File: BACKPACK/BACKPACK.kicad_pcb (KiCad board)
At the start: 4 copper layers, 70.8 x 45 mm, 30 parts, among them J1 Conn_01x03_Pin, J2 Conn_01x03_Pin, J3 Conn_01x03_Pin, J4 Conn_Coaxial, J5 Conn_02x08_Odd_Even, J6 Conn_02x08_Odd_Even, J7 Conn_01x03_Pin, SW1 BOOTSEL, SW2 RESET, U10 RAK3172, U9 TESEO-LIV4F

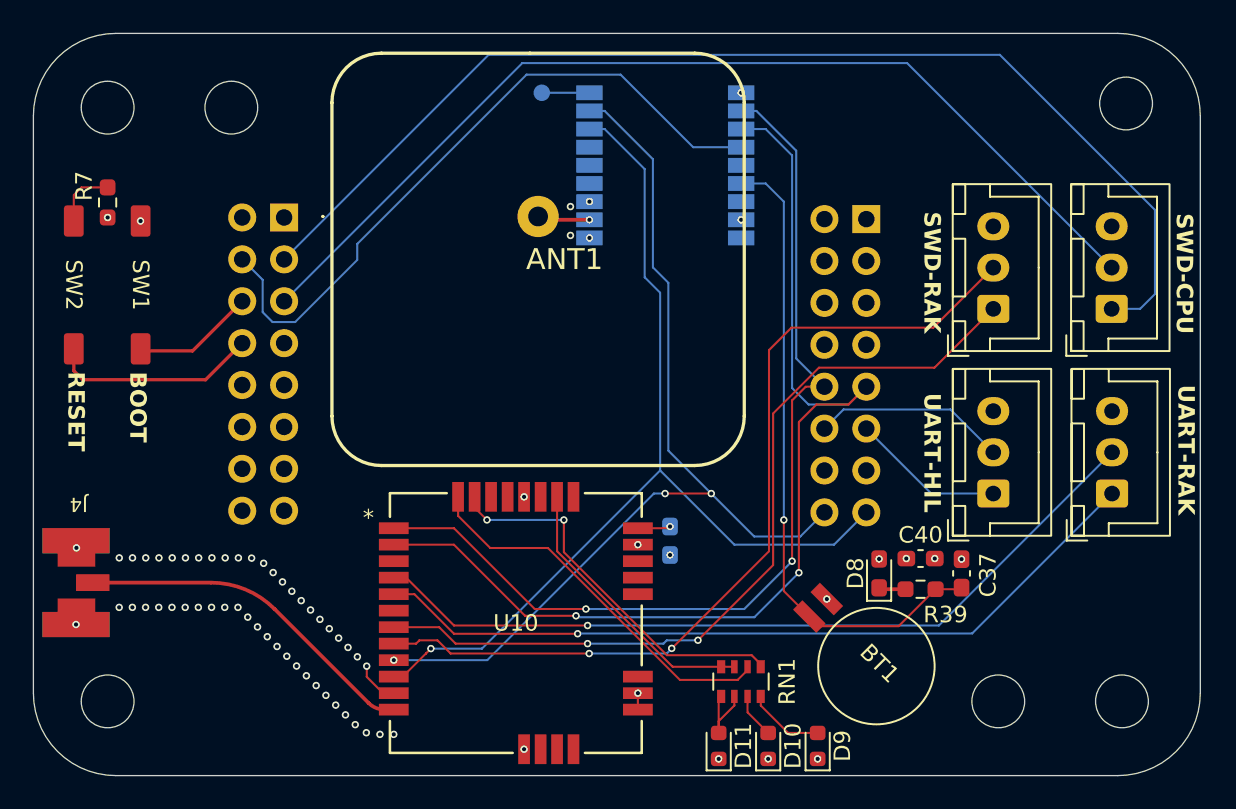
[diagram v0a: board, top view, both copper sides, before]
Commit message: constrains fix
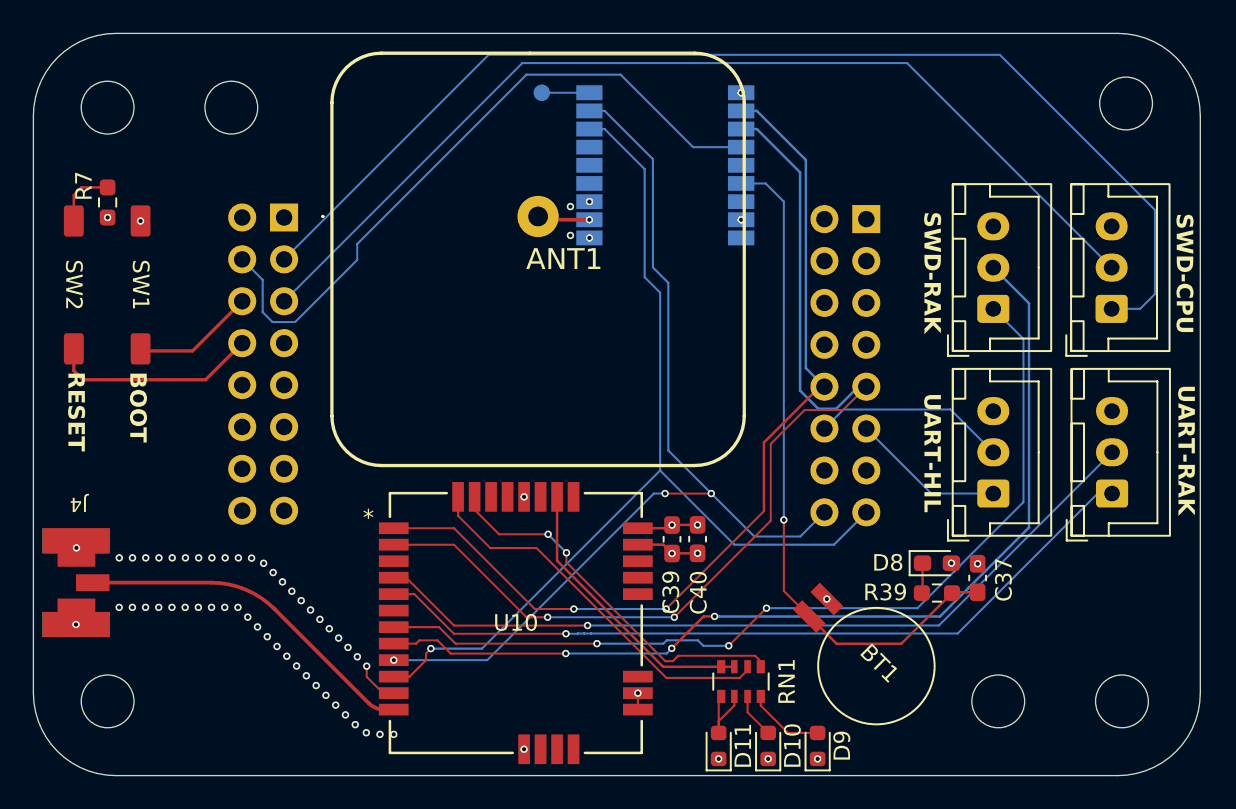
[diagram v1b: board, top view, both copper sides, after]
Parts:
- added G***: LOGO, LOGO, B.Cu at (158.1, 88.8)
- added G***: LOGO, LOGO, B.Cu at (180.2, 70.3)
- C39: moved to F.Cu
- moved C40 13.6 mm to (166.8, 96.2), turned to -90 degrees
- moved D8 3.56 mm to (181.3, 97.6), turned to 0 degrees
- moved R39 1.02 mm to (181.3, 99.4)
- moved C37 1.01 mm to (183.8, 98.5)
- moved C39 0.15 mm to (165.2, 96.2)
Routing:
- net /SWCLK: track 53.6 -> 58.7 mm, vias 2 -> 3
- net /SWDIO: track 50.6 -> 54.9 mm, vias 2 -> 3
- net GND: track 3.70 -> 7.54 mm, vias 67 -> 66
- net /TX_GPS: track 58.8 -> 55.5 mm
- net /RX_GPS: track 64.8 -> 61.9 mm
- net Net-(BT1-+): track 39.3 -> 41.0 mm
- net +3V3: track 2.15 -> 3.70 mm

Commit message: fine rev 2.2
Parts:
- H1, H2, H3, H4, H5, H6: moved to B.Cu
- J5, J6: moved to F.Cu
- moved H4 61.5 mm to (131.0, 106.0), turned to 180 degrees
- moved H3 61.0 mm to (192.0, 106.0), turned to 180 degrees
- moved H5 47.0 mm to (138.0, 106.0), turned to 180 degrees
- moved H6 46.5 mm to (185.0, 70.0), turned to 180 degrees
- moved J6 22.7 mm to (141.7, 99.3)
- moved J5 22.7 mm to (177.0, 99.4)
- moved BT1 5.88 mm to (179.5, 102.6)
- moved SW2 4.25 mm to (133.2, 80.8)
- moved SW1 3.90 mm to (129.1, 80.8)
- moved H2 0.79 mm to (192.0, 70.0), turned to 180 degrees
- turned H1 to 180 degrees
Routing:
- net /CPU_SWDIO: track 61.3 -> 80.1 mm, vias 0 -> 1
- net /CPU_SWDCLK: track 69.9 -> 87.6 mm, vias 0 -> 1
- net PPS: track 41.6 -> 54.4 mm, vias 0 -> 1
- net GND: track 7.54 -> 18.3 mm, vias 66 -> 64
- net /BOOTSEL: track 7.89 -> 15.6 mm
- net /TX_GPS: track 55.5 -> 62.6 mm
- net Net-(BT1-+): track 41.0 -> 47.8 mm
- net /RX_GPS: track 61.9 -> 59.2 mm
- net HIL_RX: track 11.8 -> 13.6 mm, vias 0 -> 1
- net /RESET: track 12.7 -> 11.2 mm
- net /SDA_RADIO: track 59.8 -> 58.5 mm, vias 1 -> 2
- net HIL_TX: track 9.33 -> 10.5 mm, vias 0 -> 1
- net ANT: track 21.1 -> 20.5 mm
- net +3V3: vias 4 -> 5

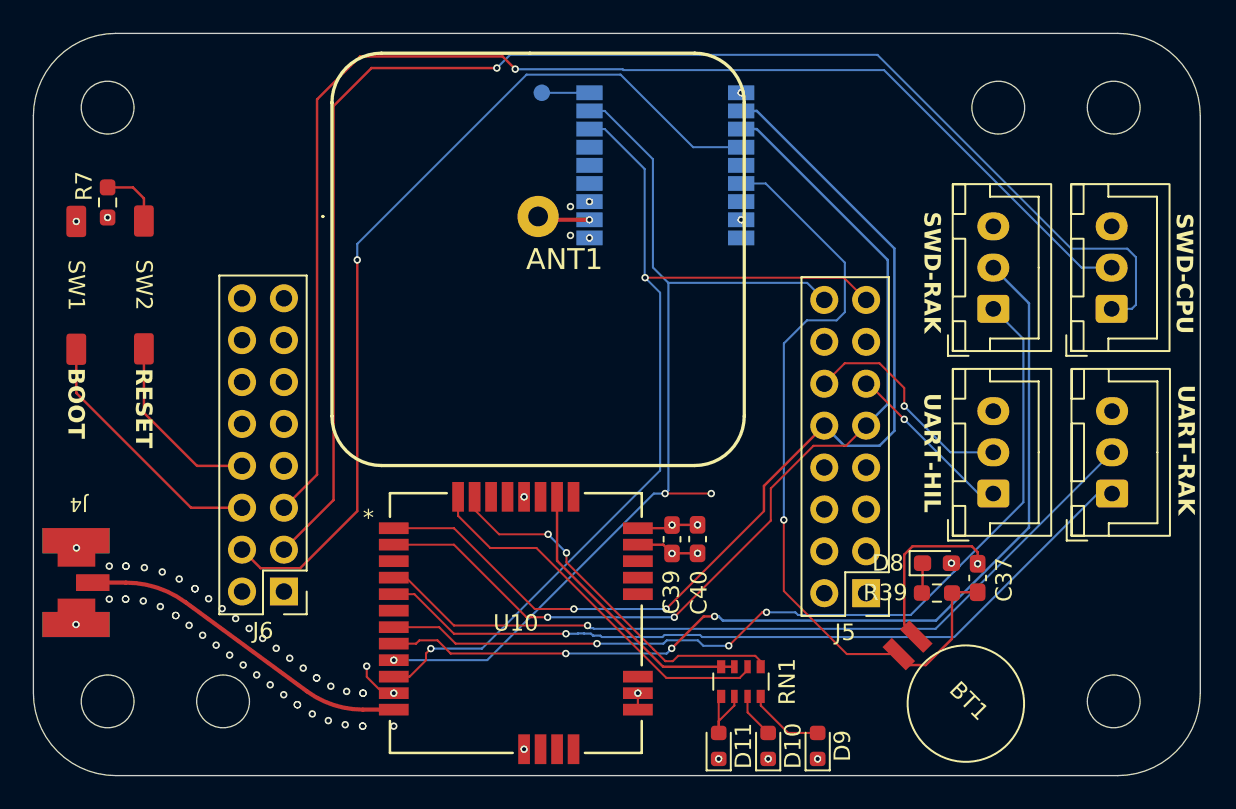
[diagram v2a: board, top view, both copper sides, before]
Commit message: Aggiunta GNDPlane
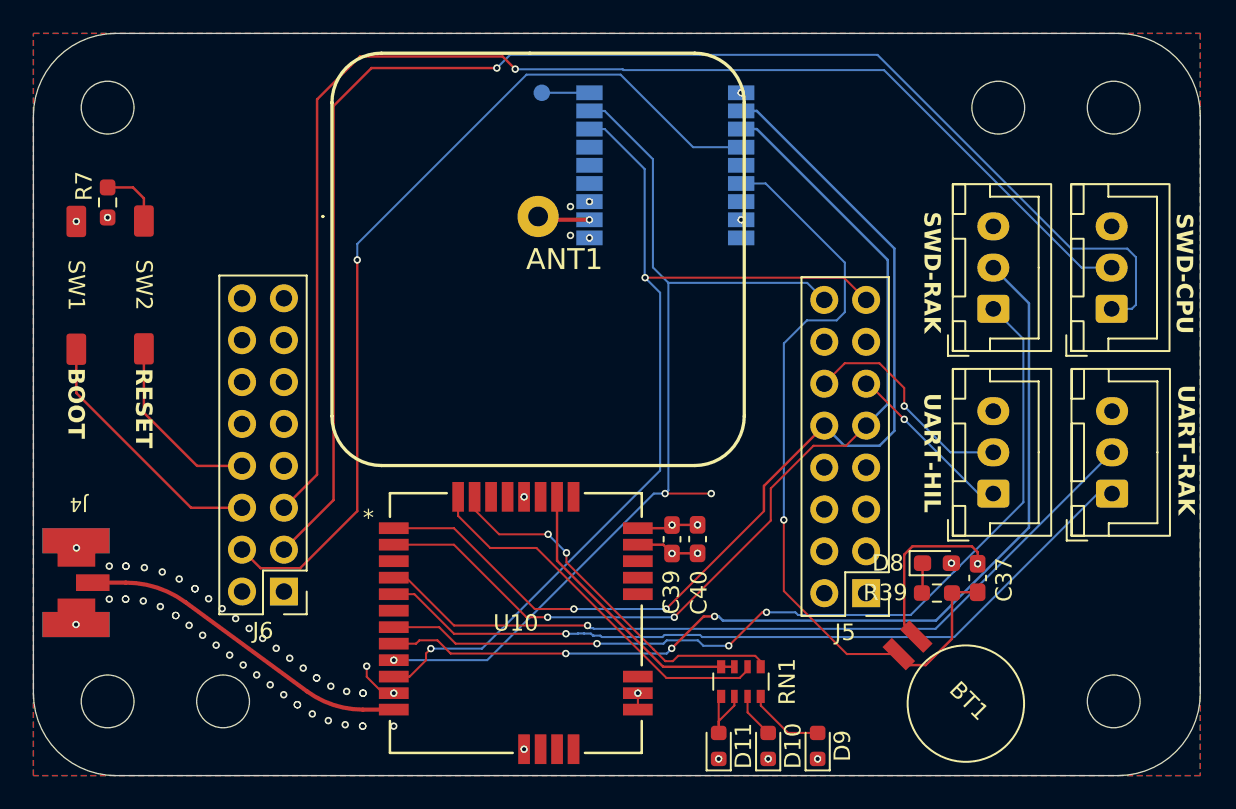
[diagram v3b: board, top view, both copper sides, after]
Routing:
- added copper zone on B.Cu, net GND
- added copper zone on F.Cu, net GND
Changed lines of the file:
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@@
+		(net 1)
+		(net_name "GND")
+		(layer "F.Cu")
+		(hatch edge 0.5)
+		(priority 2)
+		(connect_pads
+			(clearance 0.125)
+		)
+		(min_thickness 0.25)
+		(filled_areas_thickness no)
+		(fill
+			(thermal_gap 0.5)
+			(thermal_bridge_width 0.5)
+		)
+		(polygon
+			(pts
+				(xy 197.25 65.5) (xy 197.25 110.5) (xy 126.5 110.5) (xy 126.5 65.5)
+			)
+		)
+	)
+	(zone
+		(net 1)
+		(net_name "GND")
+		(layer "B.Cu")
+		(hatch edge 0.5)
+		(priority 3)
+		(connect_pads
+			(clearance 0.125)
+		)
+		(min_thickness 0.25)
+		(filled_areas_thickness no)
+		(fill
+			(thermal_gap 0.5)
+			(thermal_bridge_width 0.5)
+		)
+		(polygon
+			(pts
+				(xy 197.25 65.5) (xy 197.25 110.5) (xy 126.5 110.5) (xy 126.5 65.5)
+			)
+		)
+	)
+	(zone
 		(net 1)
 		(net_name "GND")
